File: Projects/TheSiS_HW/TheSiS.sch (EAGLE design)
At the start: 50 parts, among them IC1 REG1117, IC3 TP4056, IC4 MCP1703CB, IC5 CP2102, T1 DMN3024LSD, U1 ESP-WROOM-32, X2 ZX62D-B-5PA8

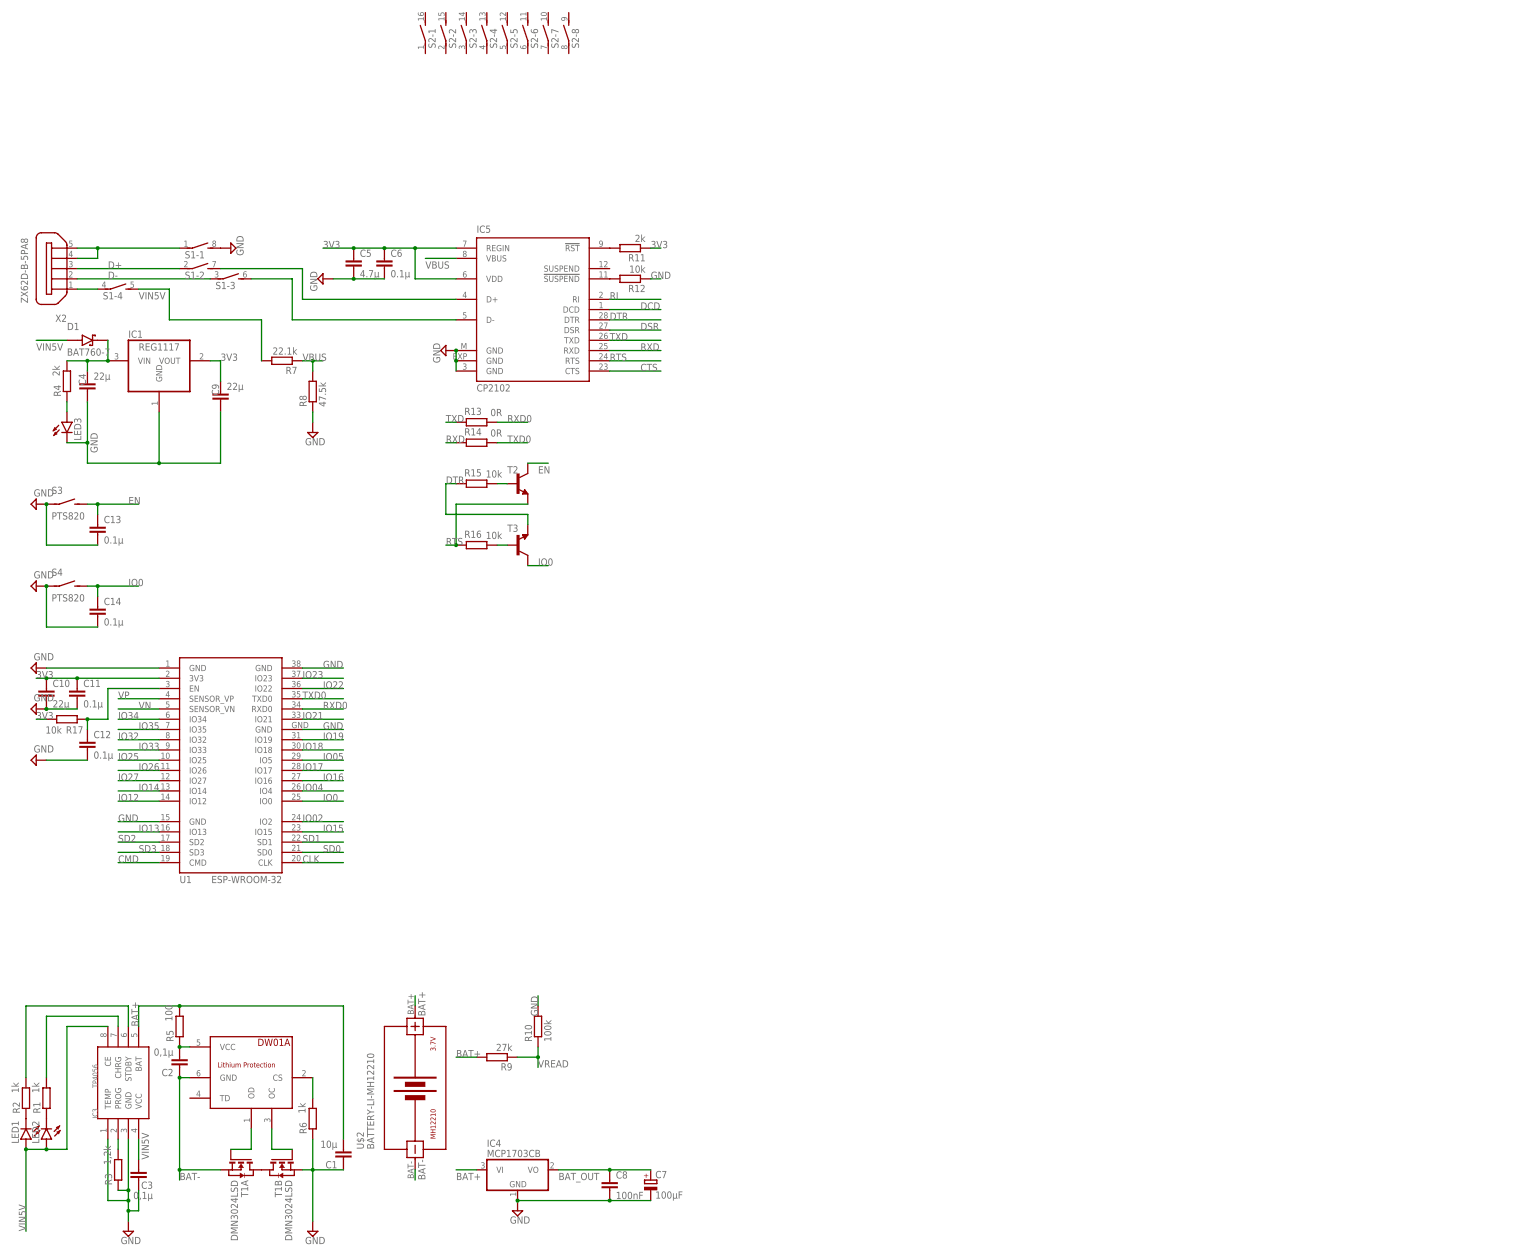
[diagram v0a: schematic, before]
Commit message: Rename HW_Design => Thesis_HW
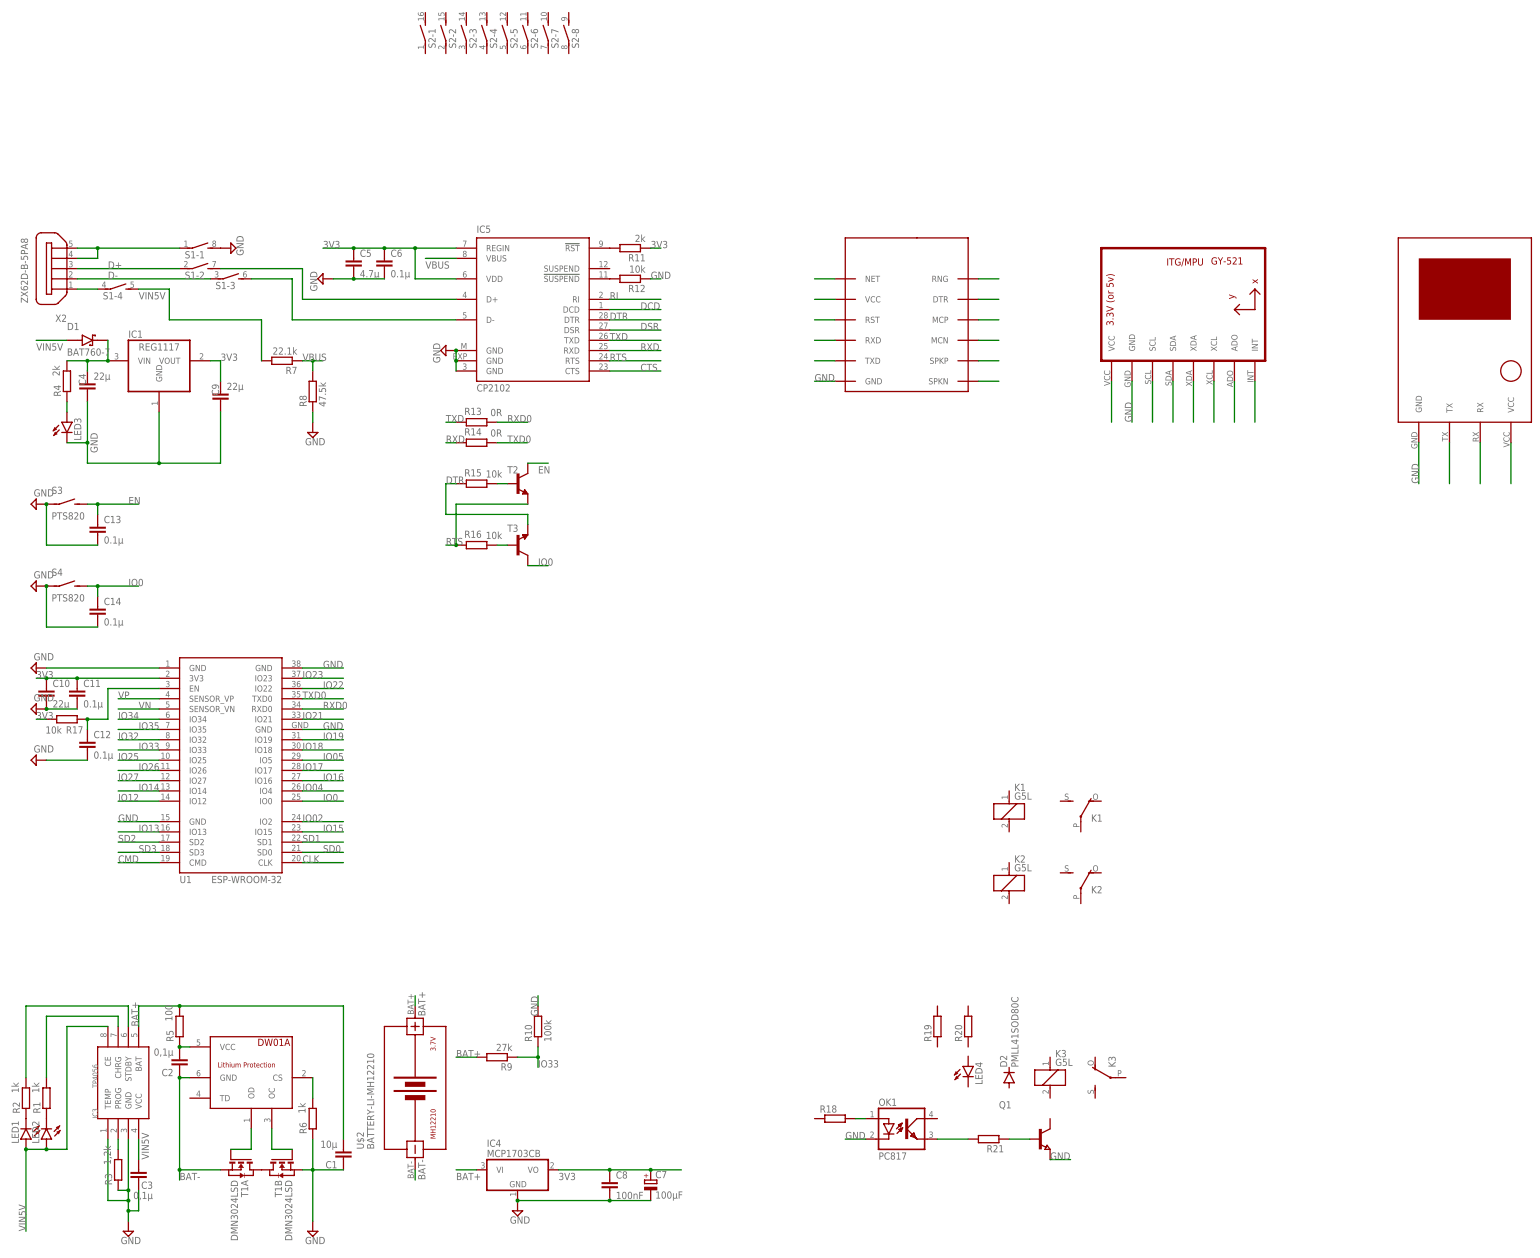
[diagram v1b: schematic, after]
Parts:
- added D2: PMLL41SOD80C, diode:PMLL41SOD80C
- added K1, K2, K3: G5L, relay:G5L
- added LED4: (no value), led:LEDCHIP-LED0805
- added OK1: PC817, optocoupler:PC817
- added Q1: (no value), semicon-smd-ipc:NPN-TRANSISTOR_SOT23
- added R18, R19, R20, R21: (no value), rcl:R-EU_R0805
- added U$3: U-BLOX-NEO6V2, u-blox neo-6m v2:U-BLOX-NEO6V2
- added U$4: SIM800L, sim800l:SIM800L
- added U2: GY-521MPU6050, gy-521:GY-521MPU6050
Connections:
- removed net BAT_OUT: C7.+, C8.1, IC4.VO
- removed net VREAD: R10.1, R9.1
- new net N$21: U$4.NET
- new net N$22: U$4.VCC
- new net N$23: U$4.RST
- new net N$24: U$4.RXD
- new net N$25: U$4.TXD
- new net N$26: OK1.A, R18.2
- new net N$27: U$4.SPKN
- new net N$28: U$4.SPKP
- new net N$29: U$4.RNG
- new net N$30: U$4.DTR
- new net N$31: U$4.MCP
- new net N$32: U$4.MCN
- new net N$33: U2.VCC
- new net N$34: OK1.EMIT, R21.2
- new net N$35: U2.SCL
- new net N$36: U2.SDA
- new net N$37: U2.XDA
- new net N$38: U2.XCL
- new net N$39: U2.ADO
- new net N$40: U2.INT
- new net N$41: Q1.B, R21.1
- new net N$42: U$3.TX
- new net N$43: U$3.RX
- new net N$44: U$3.VCC
- net 3V3: now also C7.+, C8.1, IC4.VO
- net GND: now also OK1.C, Q1.E, U$3.GND, U$4.GND, U2.GND
- net IO33: now also R10.1, R9.1

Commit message: Finish TheSiS_HW Schematic
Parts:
- added D3, D4: PMLL41SOD80C, diode:PMLL41SOD80C
- added LED5, LED6: (no value), led:LEDCHIP-LED0805
- added OK2, OK3: TLP283, optocoupler:TLP283
- added Q2, Q3: (no value), semicon-smd-ipc:NPN-TRANSISTOR_SOT23
- added R22, R26: 220, rcl:R-EU_R0805
- added R23, R24, R25, R27, R28, R29: 10k, rcl:R-EU_R0805
- added X1, X3, X4: (no value), con-wago-508:W237-03P
- OK1: value PC817 -> TLP283; device optocoupler:PC817 -> optocoupler:TLP283
- R18: value (none) -> 220
- R19, R20, R21: value (none) -> 10k
- T2, T3: SPICEPREFIX (none) -> J
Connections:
- removed net N$35: U2.SCL
- removed net N$36: U2.SDA
- new net $VCCSIM800: S2-1.2, U$4.VCC
- new net BAT_VCC: S2-4.1, S2-5.1, S2-6.1, S2-8.1, U$2.BAT+
- new net IO2: R18.1, S2-6.2
- new net IO4: R22.1, S2-5.2
- new net IO5: R26.1
- new net N$45: D2.A, K31.2, LED4.C, Q1.C, R19.1
- new net N$46: K32.O, X1-3.KL
- new net N$47: K32.P, X1-2.KL
- new net N$48: K32.S, X1-1.KL
- new net N$49: LED4.A, R20.1
- new net N$50: OK1.A, R22.2
- new net N$51: OK1.EMIT, R25.2
- new net N$52: Q2.B, R25.1
- new net N$53: D3.A, K11.2, LED5.C, Q2.C, R23.1
- new net N$54: LED5.A, R24.1
- new net N$55: K12.O, X3-3.KL
- new net N$56: K12.P, X3-2.KL
- new net N$57: K12.S, X3-1.KL
- new net N$58: D4.A, K21.2, LED6.C, Q3.C, R27.1
- new net N$59: LED6.A, R28.1
- new net N$60: K22.O, X4-3.KL
- new net N$61: K22.P, X4-2.KL
- new net N$62: K22.S, X4-1.KL
- net 3V3: now also S2-1.1
- net BAT+: now also D2.C, D3.C, D4.C, K11.1, K21.1, K31.1, OK1.COL, OK2.COL, OK3.COL, R19.2, R20.2, R23.2, R24.2, R27.2, R28.2, S2-7.1, U$3.VCC; no longer U$2.BAT+
- net GND: now also OK2.C, OK3.C, Q2.E, Q3.E
- net IO16: now also U$3.TX
- net IO17: now also U$3.RX
- net IO21: now also U2.SDA
- net IO22: now also U2.SCL
- net N$22: now also S2-7.2, S2-8.2; no longer U$4.VCC
- net N$24: now also S2-2.2
- net N$25: now also S2-3.2
- net N$26: now also OK2.A; no longer OK1.A
- net N$33: now also S2-4.2
- net N$34: now also OK2.EMIT; no longer OK1.EMIT
- net N$42: now also OK3.A, R26.2; no longer U$3.TX
- net N$43: now also OK3.EMIT, R29.2; no longer U$3.RX
- net N$44: now also Q3.B, R29.1; no longer U$3.VCC
- net RXD0: now also S2-3.1
- net TXD0: now also S2-2.1
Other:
- moved on the sheet: C1, C10, C11, C12, C13, C14, C2, C3, C4, C5, C6, C7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

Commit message: Selesai Board v20.10.21
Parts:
- removed C10: 22µ, rcl:C-EUC0805
- removed C11: 0.1µ, rcl:C-EUC0805
- removed C7: 100µF, rcl:CPOL-EUE2,5-6E
- C1: device rcl:C-EUC0603K -> rcl:C-EUC0603
- C2: device rcl:C-EUC0805K -> rcl:C-EUC0805
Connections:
- removed net IO2: R18.1, S2-6.2
- removed net IO4: R22.1, S2-5.2
- removed net IO5: R26.1
- net 3V3: no longer C10.1, C11.1, C7.+
- net BAT+: now also S2-8.1; no longer S2-7.1
- net BAT_VCC: now also S2-4.2, S2-5.2, S2-6.2, S2-7.2; no longer S2-4.1, S2-5.1, S2-6.1, S2-8.1
- net GND: now also S1-4.2; no longer C10.2, C11.2, C7.-, S1-1.2
- net IO02: now also R18.1, S2-6.1
- net IO04: now also R22.1, S2-5.1
- net IO15: now also R26.1
- net N$12: now also S1-1.1; no longer S1-4.1
- net N$15: now also S1-4.1; no longer S1-1.1
- net N$16: now also X2G$1.2; no longer X2G$1.3
- net N$17: now also X2G$1.3; no longer X2G$1.2
- net N$22: now also S2-7.1; no longer S2-7.2
- net N$24: now also U$4.TXD; no longer U$4.RXD
- net N$25: now also U$4.RXD; no longer U$4.TXD
- net N$33: now also S2-4.1; no longer S2-4.2
- net RXD0: now also S2-2.1; no longer S2-3.1
- net TXD0: now also S2-3.1; no longer S2-2.1
- net VIN5V: now also S1-1.2; no longer S1-4.2
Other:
- moved on the sheet: S1-1, S1-2, S1-3, S1-4, S2-2, S2-3, S2-4, S2-5, S2-6, S2-7, S2-8

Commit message: Finish Hardware v20.10.21
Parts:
- renumbered U$2 to 18650
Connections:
- new net EXT5V: C4.1, D1.K, IC1.VIN, R4.2
- net VIN5V: no longer C4.1, D1.K, IC1.VIN, R4.2
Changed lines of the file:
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@@
 <part name="S2" library="switch-dil" library_urn="urn:adsk.eagle:library:375" deviceset="DIP08S" device="" package3d_urn="urn:adsk.eagle:package:27257/2"/>
 <part name="U$1" library="DW01A" deviceset="DW01A" device=""/>
-<part name="U$2" library="diy-modules" deviceset="BATTERY-LI-MH12210" device=""/>
+<part name="18650" library="diy-modules" deviceset="BATTERY-LI-MH12210" device=""/>
 <part name="T1" library="FS8205A" deviceset="DMN3024LSD" device=""/>
 <part name="IC3" library="TP4056" deviceset="TP4056" device=""/>
@@
 </instance>
 <instance part="U$1" gate="G$1" x="63.5" y="55.88" smashed="yes" grouprefs="POWER_SUPPLY"/>
-<instance part="U$2" gate="G$1" x="109.22" y="48.26" smashed="yes" rot="R90" grouprefs="POWER_SUPPLY">
+<instance part="18650" gate="G$1" x="109.22" y="48.26" smashed="yes" rot="R90" grouprefs="POWER_SUPPLY">
 <attribute name="NAME" x="96.52" y="33.02" size="1.778" layer="95" rot="R90"/>
 <attribute name="VALUE" x="99.06" y="33.02" size="1.778" layer="96" rot="R90"/>
@@
 <net name="BAT-" class="0">
 <segment>
-<pinref part="U$2" gate="G$1" pin="BAT-"/>
+<pinref part="18650" gate="G$1" pin="BAT-"/>
 <wire x1="109.22" y1="27.94" x2="109.22" y2="25.4" width="0.1524" layer="91" grouprefs="POWER_SUPPLY"/>
 <label x="111.76" y="25.4" size="1.778" layer="95" rot="R90" grouprefs="POWER_SUPPLY"/>
@@
 <label x="43.18" y="30.48" size="1.778" layer="95" rot="R90" grouprefs="POWER_SUPPLY"/>
 <pinref part="C3" gate="G$1" pin="2"/>
-</segment>
-<segment>
-<pinref part="IC1" gate="G$1" pin="VIN"/>
-<pinref part="R4" gate="G$1" pin="2"/>
-<wire x1="17.78" y1="121.92" x2="22.86" y2="121.92" width="0.1524" layer="91" grouprefs="LDO_REGULATOR"/>
-<pinref part="C4" gate="G$1" pin="1"/>
-<wire x1="22.86" y1="121.92" x2="27.94" y2="121.92" width="0.1524" layer="91" grouprefs="LDO_REGULATOR"/>
-<wire x1="22.86" y1="119.38" x2="22.86" y2="121.92" width="0.1524" layer="91" grouprefs="LDO_REGULATOR"/>
-<junction x="22.86" y="121.92" grouprefs="LDO_REGULATOR"/>
-<pinref part="D1" gate="G$1" pin="K"/>
-<wire x1="27.94" y1="127" x2="27.94" y2="121.92" width="0.1524" layer="91" grouprefs="LDO_REGULATOR"/>
-<junction x="27.94" y="121.92" grouprefs="LDO_REGULATOR"/>
 </segment>
 <segment>
@@
 <net name="BAT_VCC" class="0">
 <segment>
-<pinref part="U$2" gate="G$1" pin="BAT+"/>
+<pinref part="18650" gate="G$1" pin="BAT+"/>
 <label x="109.22" y="78.74" size="1.778" layer="95" rot="R270"/>
 <pinref part="S2" gate="-7" pin="2"/>
@@
 </segment>
 </net>
+<net name="EXT5V" class="0">
+<segment>
+<pinref part="IC1" gate="G$1" pin="VIN"/>
+<pinref part="R4" gate="G$1" pin="2"/>
+<wire x1="17.78" y1="121.92" x2="22.86" y2="121.92" width="0.1524" layer="91" grouprefs="LDO_REGULATOR"/>
+<pinref part="C4" gate="G$1" pin="1"/>
+<wire x1="22.86" y1="121.92" x2="27.94" y2="121.92" width="0.1524" layer="91" grouprefs="LDO_REGULATOR"/>
+<wire x1="22.86" y1="119.38" x2="22.86" y2="121.92" width="0.1524" layer="91" grouprefs="LDO_REGULATOR"/>
+<junction x="22.86" y="121.92" grouprefs="LDO_REGULATOR"/>
+<label x="30.48" y="121.92" size="1.778" layer="95" rot="R270"/>
+<pinref part="D1" gate="G$1" pin="K"/>
+<wire x1="27.94" y1="127" x2="27.94" y2="121.92" width="0.1524" layer="91"/>
+<junction x="27.94" y="121.92"/>
+</segment>
+</net>

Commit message: Finish Board v20.10.20 [Order PCBWay.com]
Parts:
- removed U$3: U-BLOX-NEO6V2, u-blox neo-6m v2:U-BLOX-NEO6V2
- removed U2: GY-521MPU6050, gy-521:GY-521MPU6050
- added JP1, SV1: (no value), pinhead:PINHD-1X4
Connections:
- removed net N$33: S2-4.1, U2.VCC
- removed net N$37: U2.XDA
- removed net N$38: U2.XCL
- removed net N$39: U2.ADO
- removed net N$40: U2.INT
- new net N$35: JP1.1, S2-4.1
- net BAT+: now also SV1.1; no longer U$3.VCC
- net GND: now also JP1.2, SV1.4; no longer U$3.GND, U2.GND
- net IO16: now also SV1.3; no longer U$3.TX
- net IO17: now also SV1.2; no longer U$3.RX
- net IO21: now also JP1.4; no longer U2.SDA
- net IO22: now also JP1.3; no longer U2.SCL
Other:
- moved on the sheet: S2-1, S2-2, S2-3, S2-4
